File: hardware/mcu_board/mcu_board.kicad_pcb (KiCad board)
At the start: 2 copper layers, 27.2 x 54.8 mm, 9 parts, among them J1 Light, J2 Conn_ESP32-H2_Super-Mini_-_Pi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, J3 Touch, J4 Input

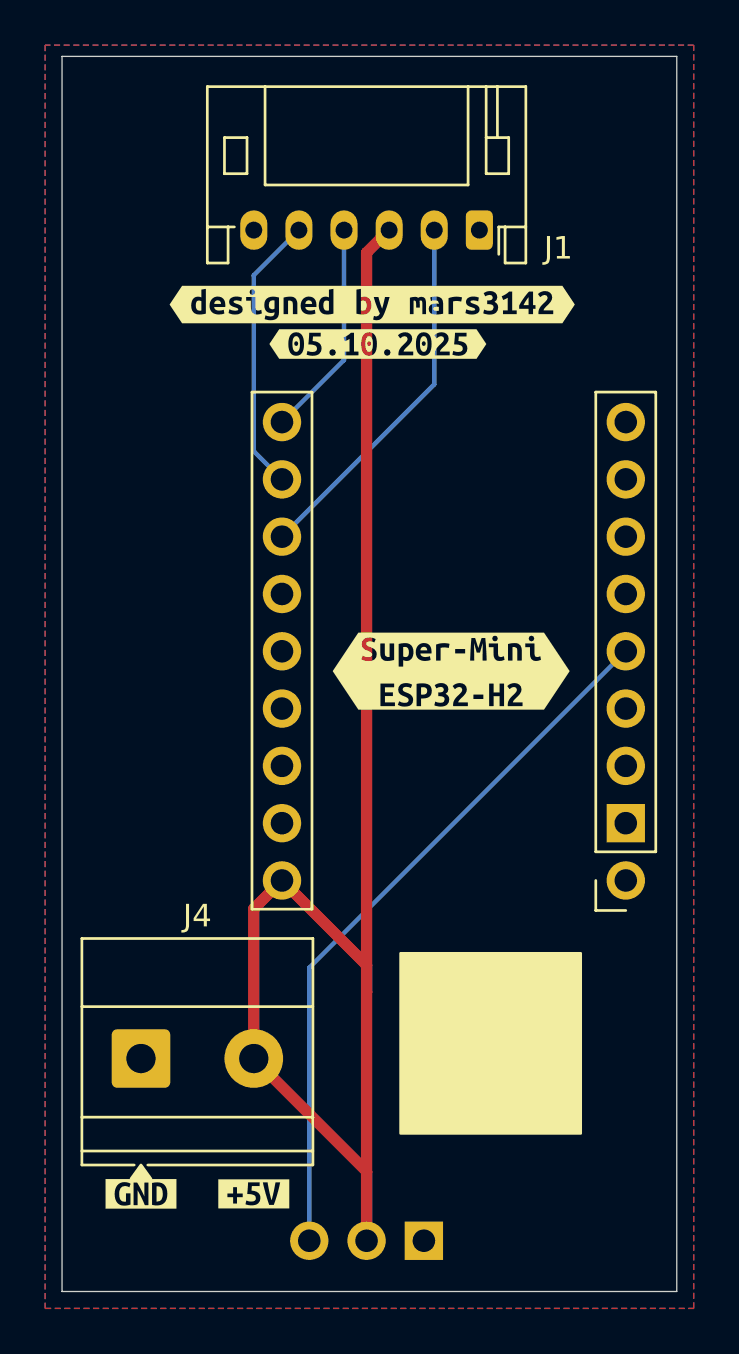
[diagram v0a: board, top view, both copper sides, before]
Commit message: latest mcu_board revision
added buck converter

Signed-off-by: Peter Siegmund <mars3142@users.noreply.github.com>
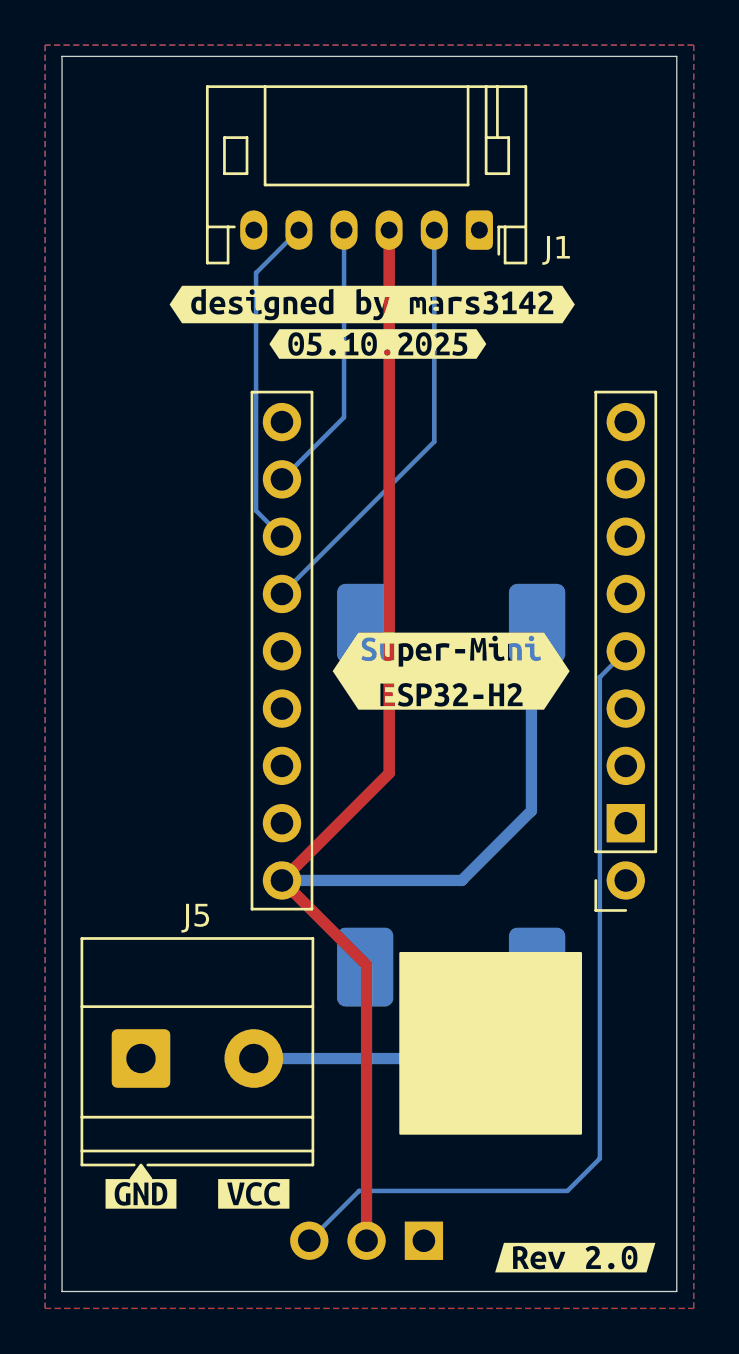
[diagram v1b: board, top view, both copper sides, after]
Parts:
- removed kibuzzard-6876C026: G***, kibuzzard-6876C026
- added J2: Buck Converter, aliexpress:Buck Converter (30V to 5V), B.Cu at (105.8, 75.0)
- added kibuzzard-68B8583C: G***, kibuzzard-68B8583C, F.Cu at (97.0, 92.7)
- added kibuzzard-68B98DAB: G***, kibuzzard-68B98DAB, F.Cu at (111.2, 95.5)
- renumbered J2 to J3, J3 to J4, J4 to J5
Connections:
- J3 pad 15: unconnected-(J2-GP12-Pad15) -> OUTDOOR_L
- J3 pad 16: OUTDOOR_L -> OUTDOOR_R
- J3 pad 17: OUTDOOR_R -> BEACON
- J3 pad 18: BEACON -> unconnected-(J3-GP9-Pad18)
- J5 pad 2: +5V -> VCC
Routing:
- net VCC: track 0.00 -> 14.5 mm
- net IO: track 32.0 -> 37.4 mm
- net OUTDOOR_L: track 16.4 -> 18.9 mm
- net BEACON: track 9.65 -> 12.2 mm
- net OUTDOOR_R: track 12.4 -> 14.9 mm
- net +5V: track 70.3 -> 69.1 mm

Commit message: add sponsor to PCBs
Signed-off-by: Peter Siegmund <mars3142@users.noreply.github.com>
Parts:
- added G***: LOGO, LOGO, F.Cu at (109.2, 90.5)

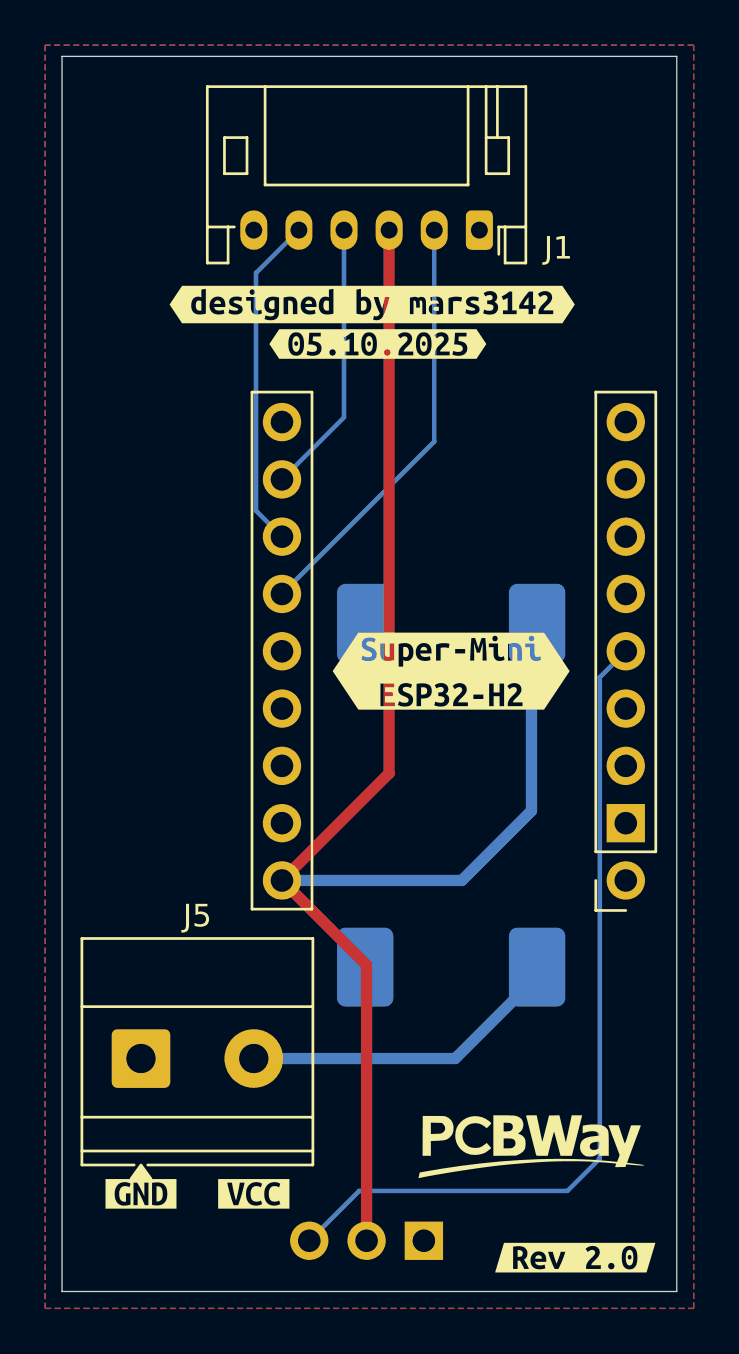
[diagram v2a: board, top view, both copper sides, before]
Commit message: new mcu board design
Signed-off-by: Peter Siegmund <mars3142@users.noreply.github.com>
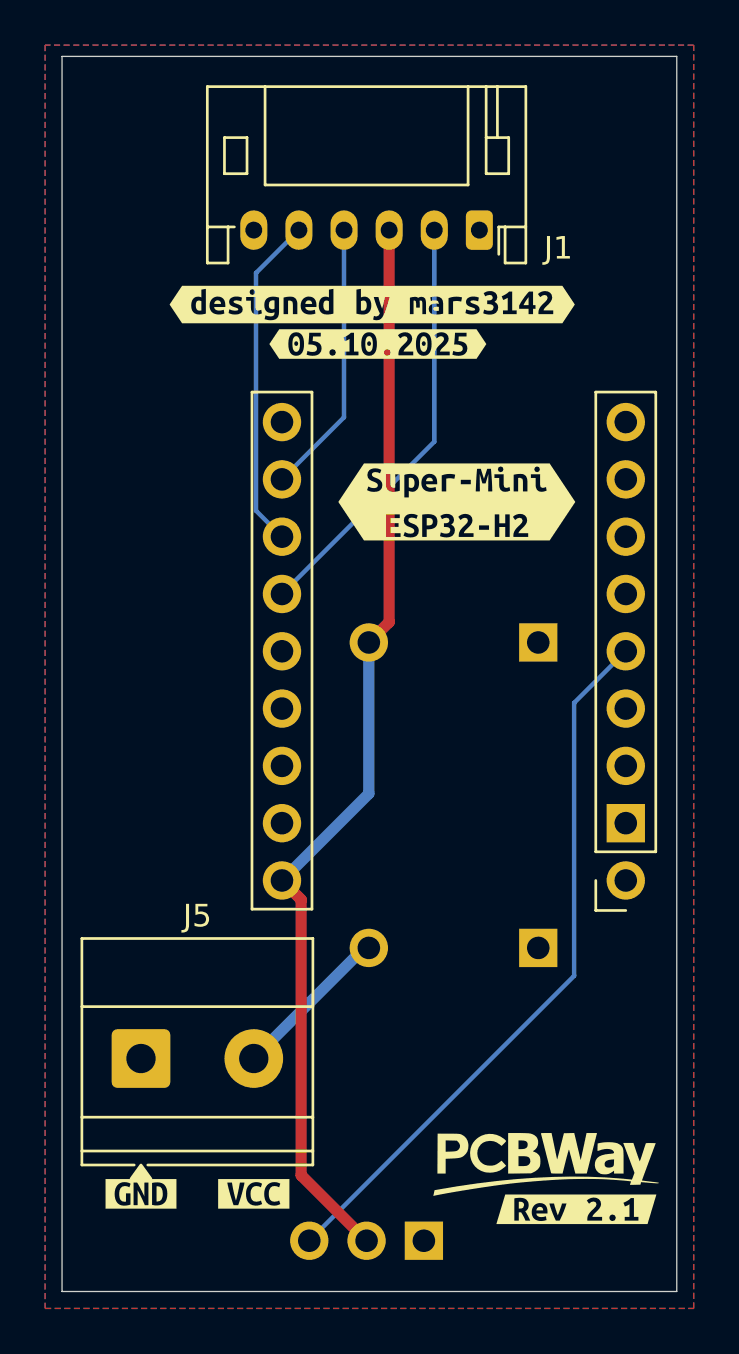
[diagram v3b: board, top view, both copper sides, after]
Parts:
- removed J2: Buck Converter, aliexpress:Buck Converter (30V to 5V)
- removed kibuzzard-68B98DAB: G***, kibuzzard-68B98DAB
- added J6: ~, aliexpress:Buck Converter (30V to 5V), B.Cu at (105.9, 75.0)
- added kibuzzard-68C9998D: G***, kibuzzard-68C9998D, F.Cu at (111.3, 93.4)
- moved kibuzzard-689F9361 7.50 mm to (106.0, 62.0)
- moved G*** 1.03 mm to (109.9, 91.3)
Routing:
- net +5V: track 69.1 -> 48.3 mm
- net VCC: track 14.5 -> 7.13 mm
- net IO: track 37.4 -> 32.0 mm
